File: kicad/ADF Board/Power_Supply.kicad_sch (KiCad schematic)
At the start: 23 parts, among them IC1 LT1054IDWG4, IC8 NCV4276CDS33R4G

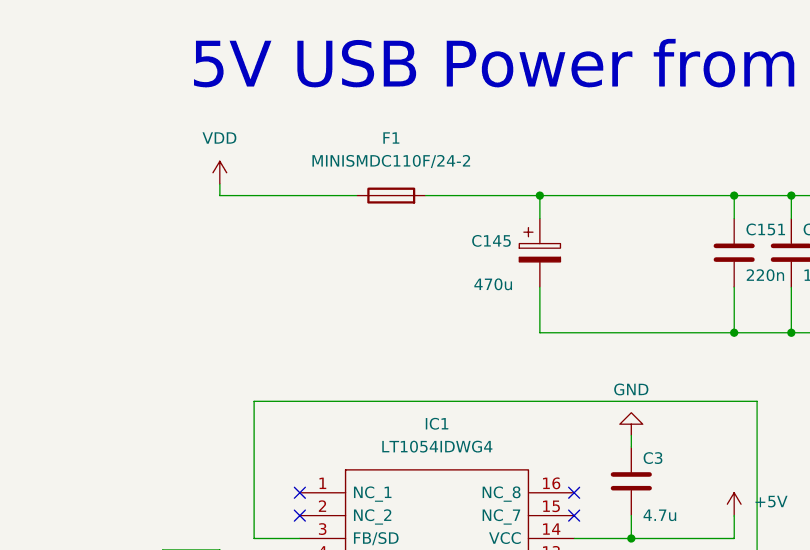
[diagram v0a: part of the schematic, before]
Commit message: Did board setup for JLC
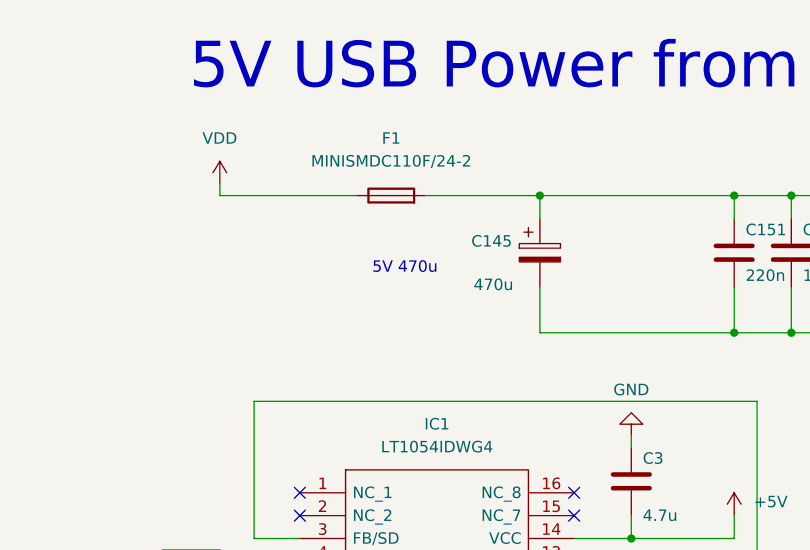
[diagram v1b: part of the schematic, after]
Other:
- note added: "5V 470u"
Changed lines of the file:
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@@
+		)
+	)
+	(text "5V 470u"
+		(exclude_from_sim no)
+		(at 52.324 41.148 0)
+		(effects
+			(font
+				(size 1.27 1.27)
+			)
 		)
 	)

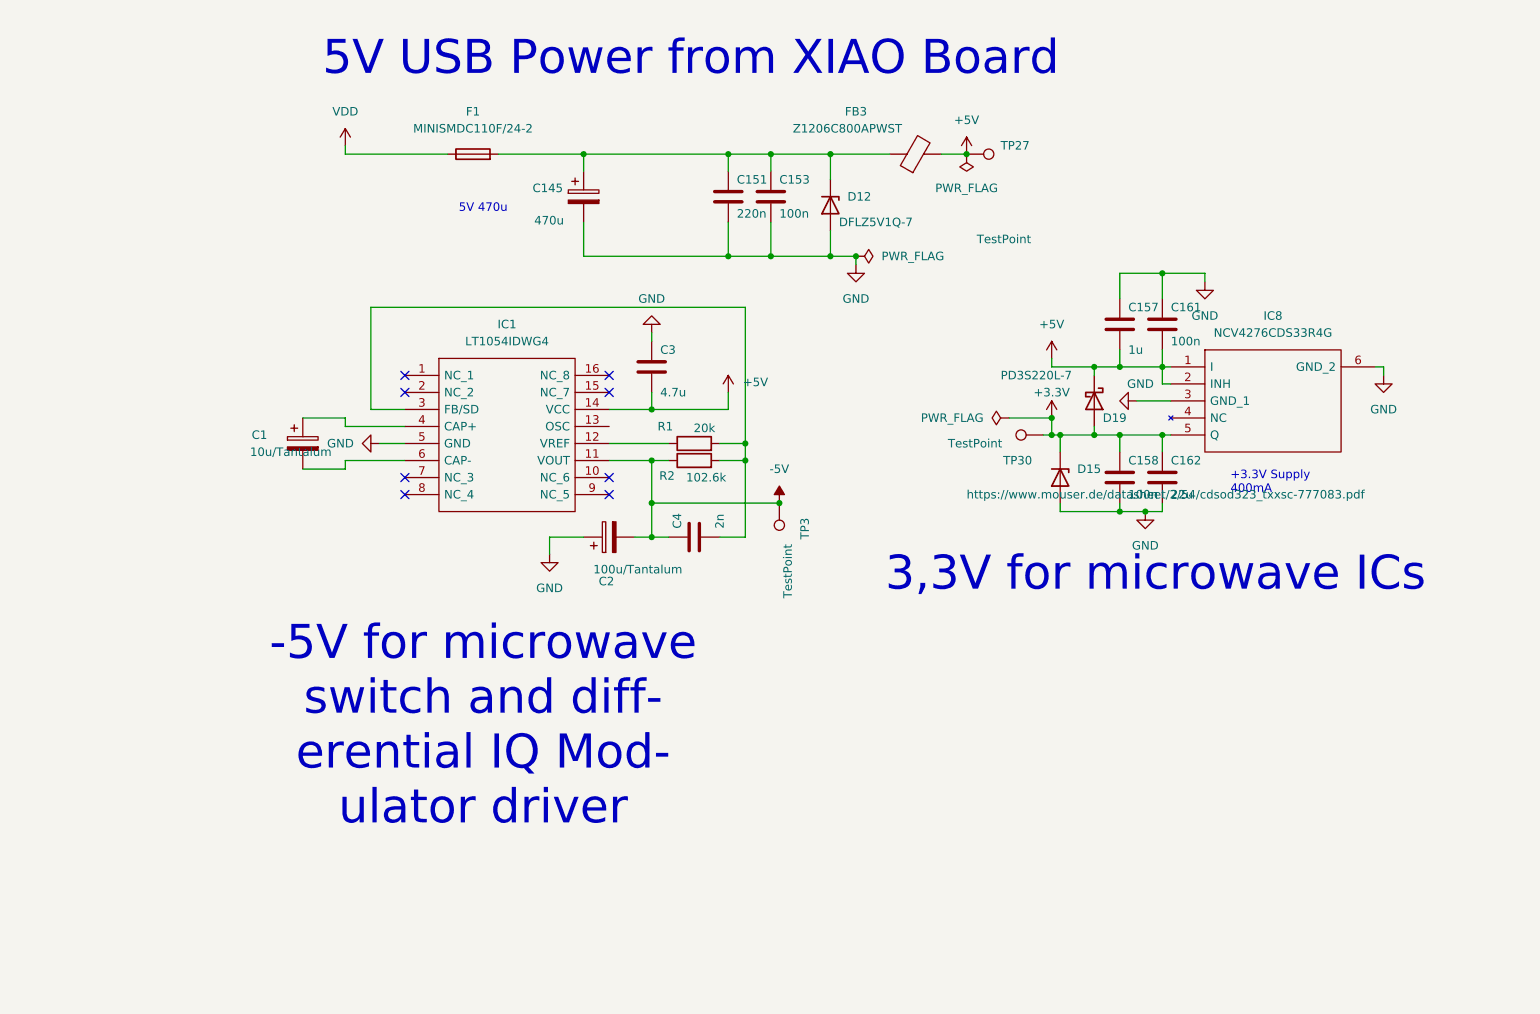
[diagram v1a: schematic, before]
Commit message: Started parts selection for assemblability Considering deleting the I/Q modulator and periphery
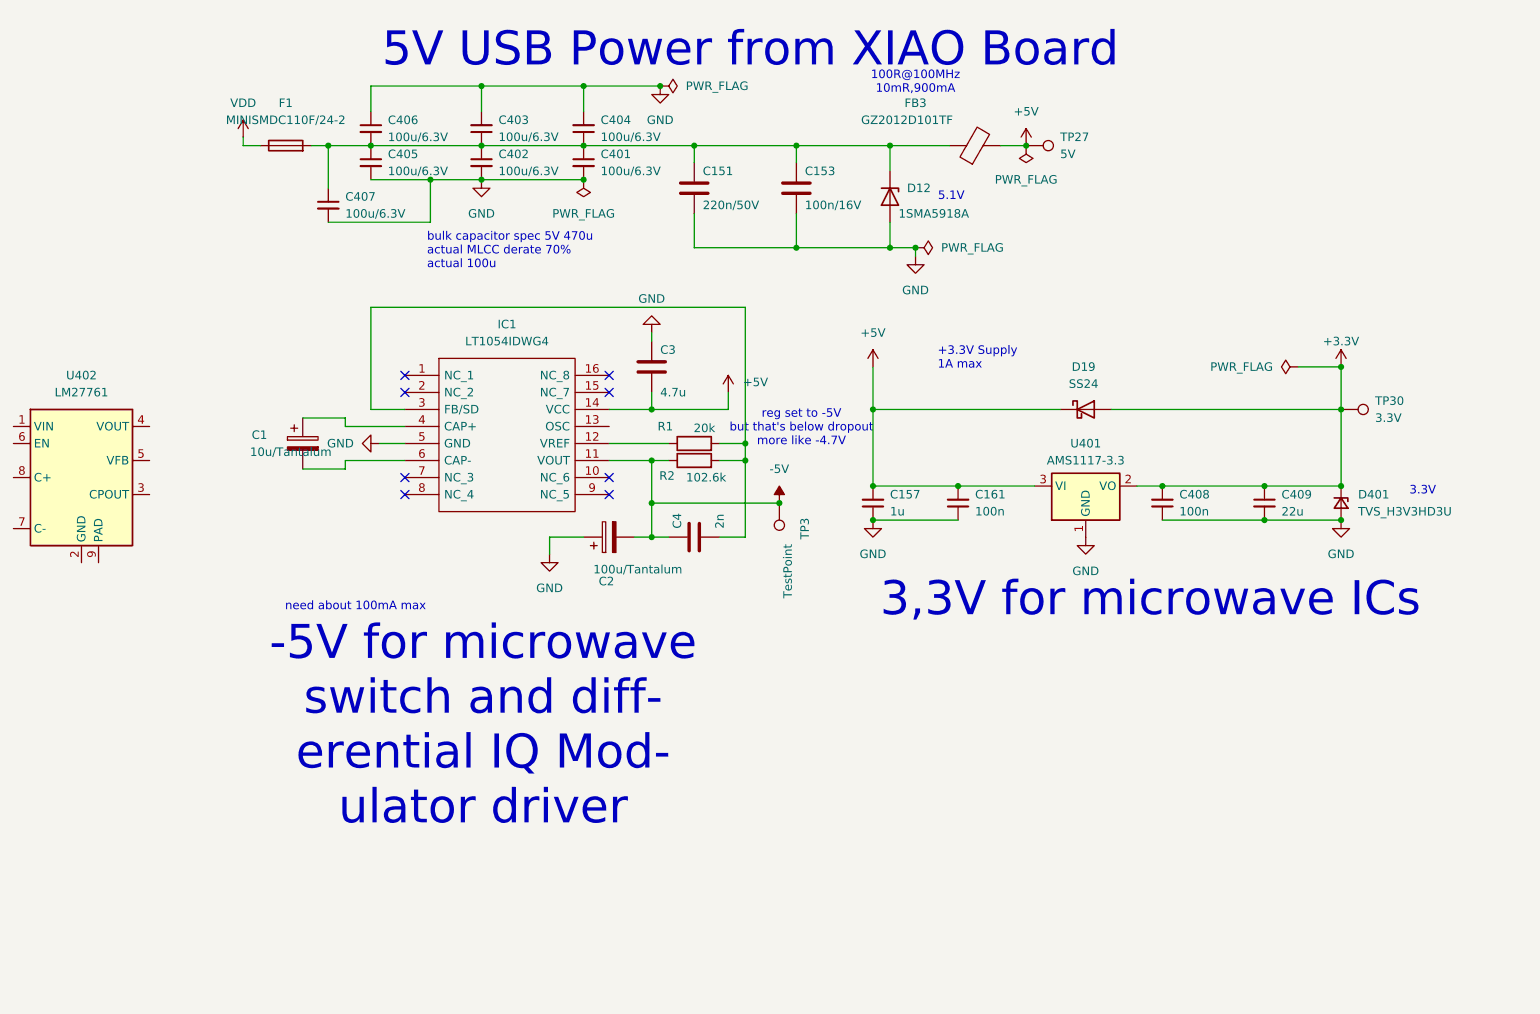
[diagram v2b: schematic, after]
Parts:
- removed C145: 470u, Capacitor_SMD:CP_Elec_8x10.5, symbol Device:C_Polarized
- removed C158: 100n, Capacitor_SMD:C_0805_2012Metric, symbol Device:C
- removed C162: 22u, Capacitor_SMD:C_1210_3225Metric, symbol Device:C
- removed D15: https://www.mouser.de/datasheet/2/54/cdsod323_txx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, Diode_SMD:D_SOD-323, symbol Device:D_Zener
- removed IC8: NCV4276CDS33R4G, SamacSys_Parts:NCV4276CDS33R4G, symbol SamacSys_Parts:NCV4276CDS33R4G
- added C401, C402, C403, C404, C405, C406, C407: 100u/6.3V, Capacitor_SMD:C_1206_3216Metric, symbol Device:C_Small
- added C408: 100n, Capacitor_SMD:C_0805_2012Metric, symbol Device:C_Small
- added C409: 22u, symbol Device:C_Small
- added D401: TVS_H3V3HD3U, Diode_SMD:D_SOD-323, symbol Device:D_Zener_Small
- added U401: AMS1117-3.3, Package_TO_SOT_SMD:SOT-223-3_TabPin2, symbol Regulator_Linear:AMS1117-3.3
- added U402: LM27761, Package_SON:WSON-8-1EP_2x2mm_P0.5mm_EP0.9x1.6mm, symbol Regulator_SwitchedCapacitor:LM27761
- C151: value 220n -> 220n/50V; footprint Capacitor_SMD:C_1206_3216Metric -> Capacitor_SMD:C_0805_2012Metric; LCSC (none) -> C5378
- C153: value 100n -> 100n/16V; footprint Capacitor_SMD:C_1206_3216Metric -> Capacitor_SMD:C_0402_1005Metric; LCSC (none) -> C1525
- C157, C161: symbol Device:C -> Device:C_Small
- D12: value DFLZ5V1Q-7 -> 1SMA5918A; footprint Diode_SMD:D_SOD-123 -> Diode_SMD:D_SMA; LCSC (none) -> C19077487
- D19: value PD3S220L-7 -> SS24; footprint SamacSys_Parts:PD3S1407 -> Diode_SMD:D_SMA; LCSC (none) -> C7420362
- FB3: value Z1206C800APWST -> GZ2012D101TF; footprint Inductor_SMD:L_1206_3216Metric -> Inductor_SMD:L_0805_2012Metric; LCSC (none) -> C1015
- TP27: value TestPoint -> 5V
- TP30: value TestPoint -> 3.3V
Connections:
- net +3.3V: now also C408.2, C409.1, D401.1 (K), U401.2 (VO)
- net +5V: now also U401.3 (VI)
- net GND: now also C401.2, C402.2, C403.2, C404.2, C405.2, C406.1, C407.2, C408.1, C409.2, D401.2 (A), U401.1 (GND)
- net at C151.1, C153.1, D12.1 (K)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: now also C401.1, C402.1, C403.1, C404.1, C405.1, C406.2, C407.1
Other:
- note added: "+3.3V Supply 1A max"
- note added: "100R@100MHz 10mR,900mA"
- note added: "3.3V"
- note added: "5.1V"
- note added: "bulk capacitor spec 5V 470u actual MLCC derate 70% actual 100u"
- note added: "need about 100mA max"
- note added: "reg set to -5V but that's below dropout more like -4.7V"
- note removed: "+3.3V Supply 400mA"
- note removed: "5V 470u"
- moved on the sheet: C151, C153, C157, C161, D12, D19, F1, FB3, TP27, TP30

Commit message: Finished part selection and rearranged schematic
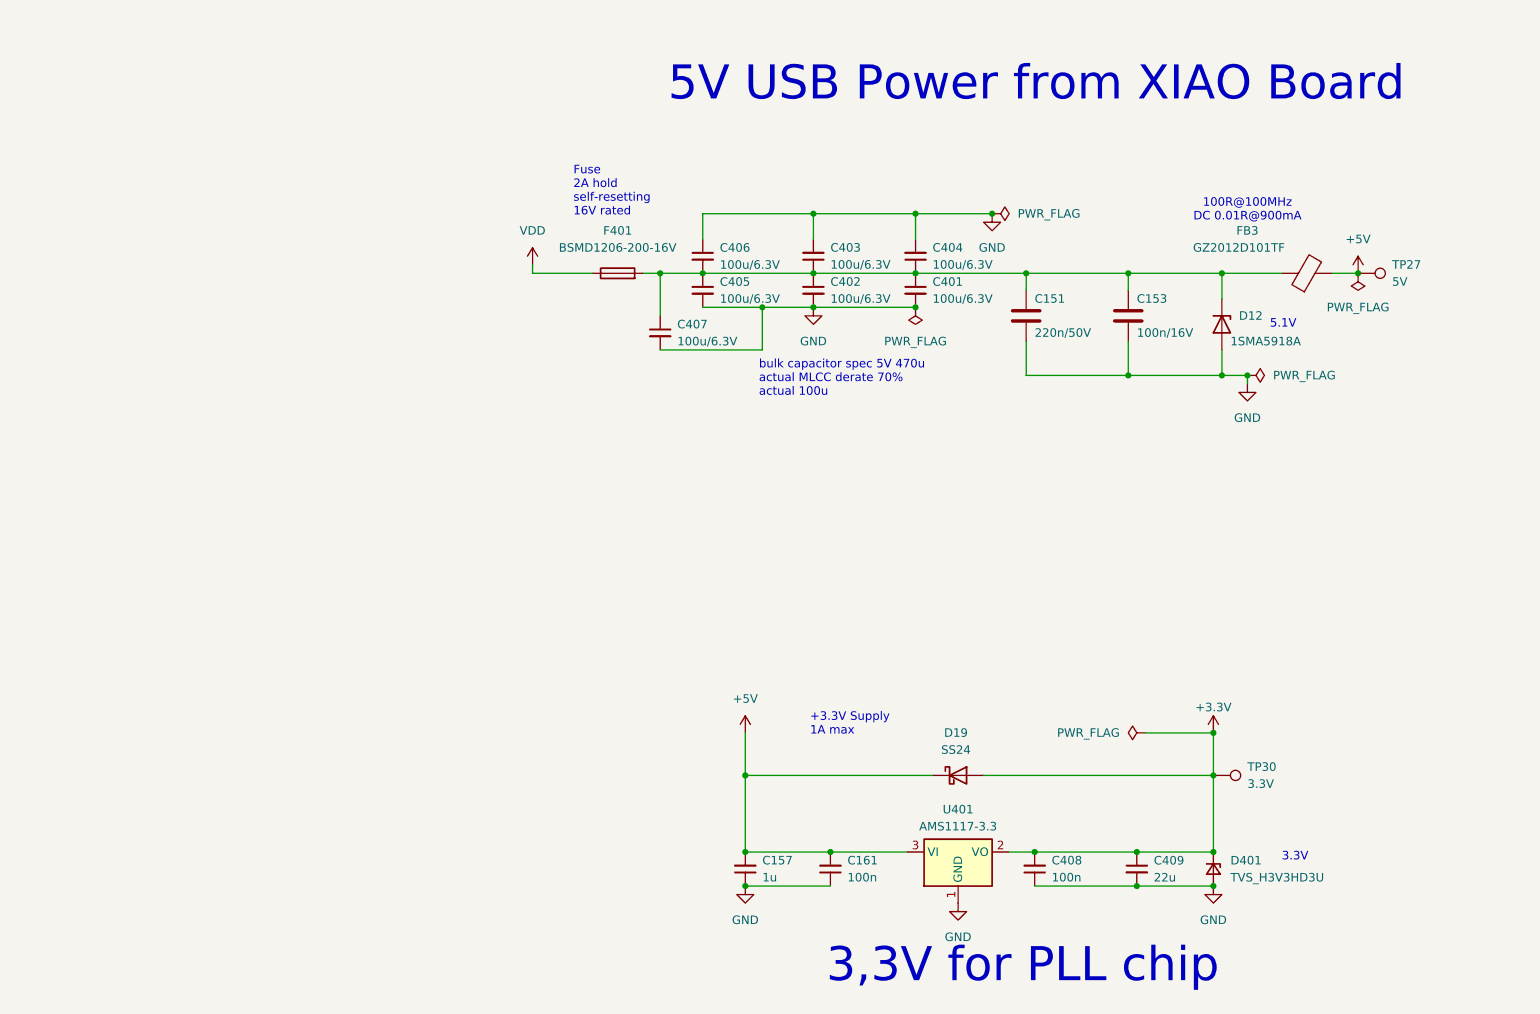
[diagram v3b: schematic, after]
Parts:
- removed C1: 10u/Tantalum, Capacitor_Tantalum_SMD:CP_EIA-6032-15_Kemet-U, symbol Device:C_Polarized
- removed C2: 100u/Tantalum, Capacitor_Tantalum_SMD:CP_EIA-7343-20_Kemet-V, symbol Device:C_Polarized
- removed C3: 4.7u, Capacitor_SMD:C_0805_2012Metric, symbol Device:C
- removed C4: 2n, Capacitor_SMD:C_0603_1608Metric, symbol Device:C
- removed F1: MINISMDC110F/24-2, Fuse:Fuse_1812_4532Metric, symbol Device:Fuse
- removed IC1: LT1054IDWG4, SamacSys_Parts:SOIC127P1030X265-16N, symbol SamacSys_Parts:LT1054IDWG4
- removed R1: 20k, Resistor_SMD:R_0603_1608Metric, symbol Device:R
- removed R2: 102.6k, Resistor_SMD:R_0603_1608Metric, symbol Device:R
- removed TP3: TestPoint, TestPoint:TestPoint_Pad_D2.0mm, symbol Connector:TestPoint
- removed U402: LM27761, Package_SON:WSON-8-1EP_2x2mm_P0.5mm_EP0.9x1.6mm, symbol Regulator_SwitchedCapacitor:LM27761
- added F401: BSMD1206-200-16V, Fuse:Fuse_1206_3216Metric, symbol Device:Fuse
- C157: footprint Capacitor_SMD:C_1206_3216Metric -> Capacitor_SMD:C_0805_2012Metric; LCSC (none) -> C28323
- C161, C408: footprint Capacitor_SMD:C_0805_2012Metric -> Capacitor_SMD:C_0402_1005Metric; LCSC (none) -> C1525
- C409: footprint (none) -> Capacitor_SMD:C_0805_2012Metric; LCSC (none) -> C45783
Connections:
- net VDD: now also F401.1
- net at C151.1, C153.1, C401.1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: now also F401.2
- no-connect marks 8 -> 0
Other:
- note added: "100R@100MHz DC 0.01R@900mA"
- note added: "3,3V for PLL chip"
- note added: "Fuse 2A hold self-resetting 16V rated"
- note removed: "-5V for microwave switch and diff- erential IQ Mod- ulator driver"
- note removed: "100R@100MHz 10mR,900mA"
- note removed: "3,3V for microwave ICs"
- note removed: "need about 100mA max"
- note removed: "reg set to -5V but that's below dropout more like -4.7V"
- moved on the sheet: C151, C153, C157, C161, C401, C402, C403, C404, C405, C406, C407, C408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
